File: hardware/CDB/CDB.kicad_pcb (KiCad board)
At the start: 2 copper layers, 17 parts, among them J1 Servo Motor, J2 Bateria, J3 Antena LoRa, Q1 BC547, U1 ESP32-C3, U2 RFM95W, U3 GPS, U4 BMP280, U5 GY-521

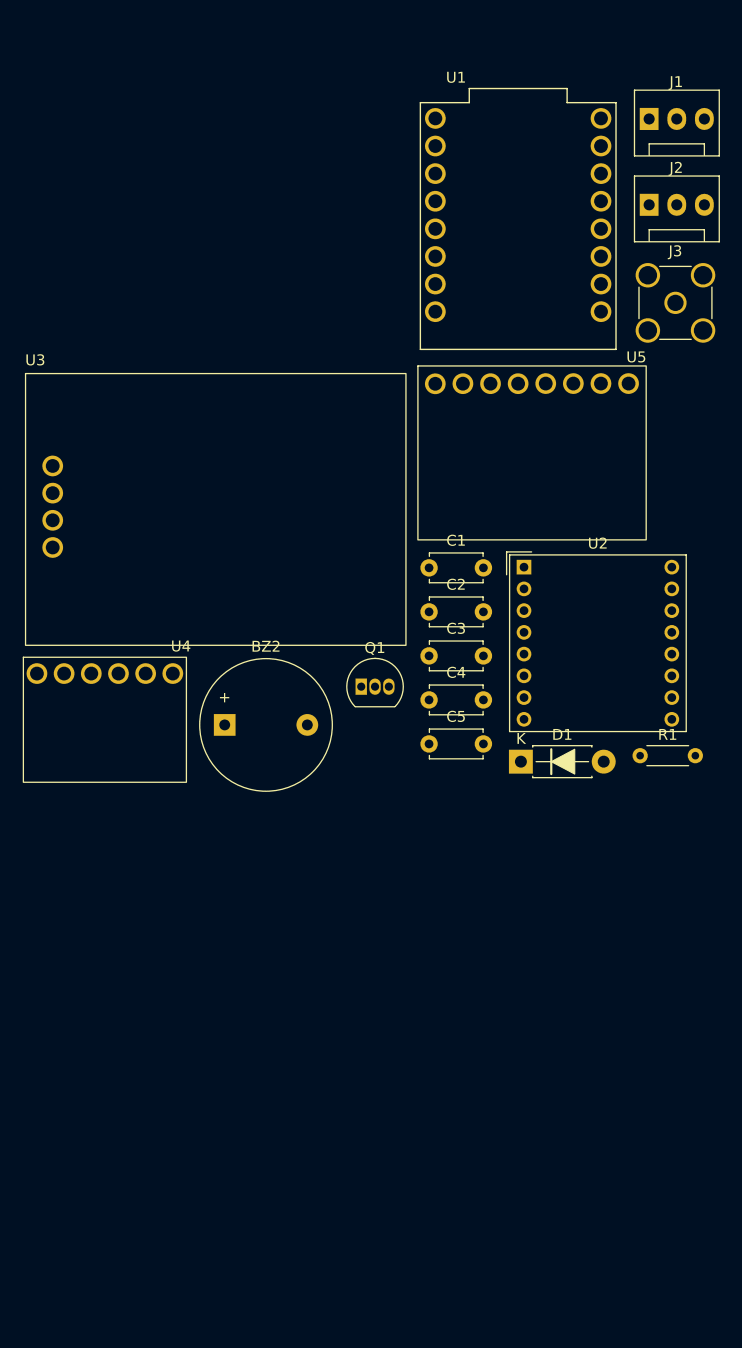
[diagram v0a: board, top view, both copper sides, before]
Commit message: add velocity threshold
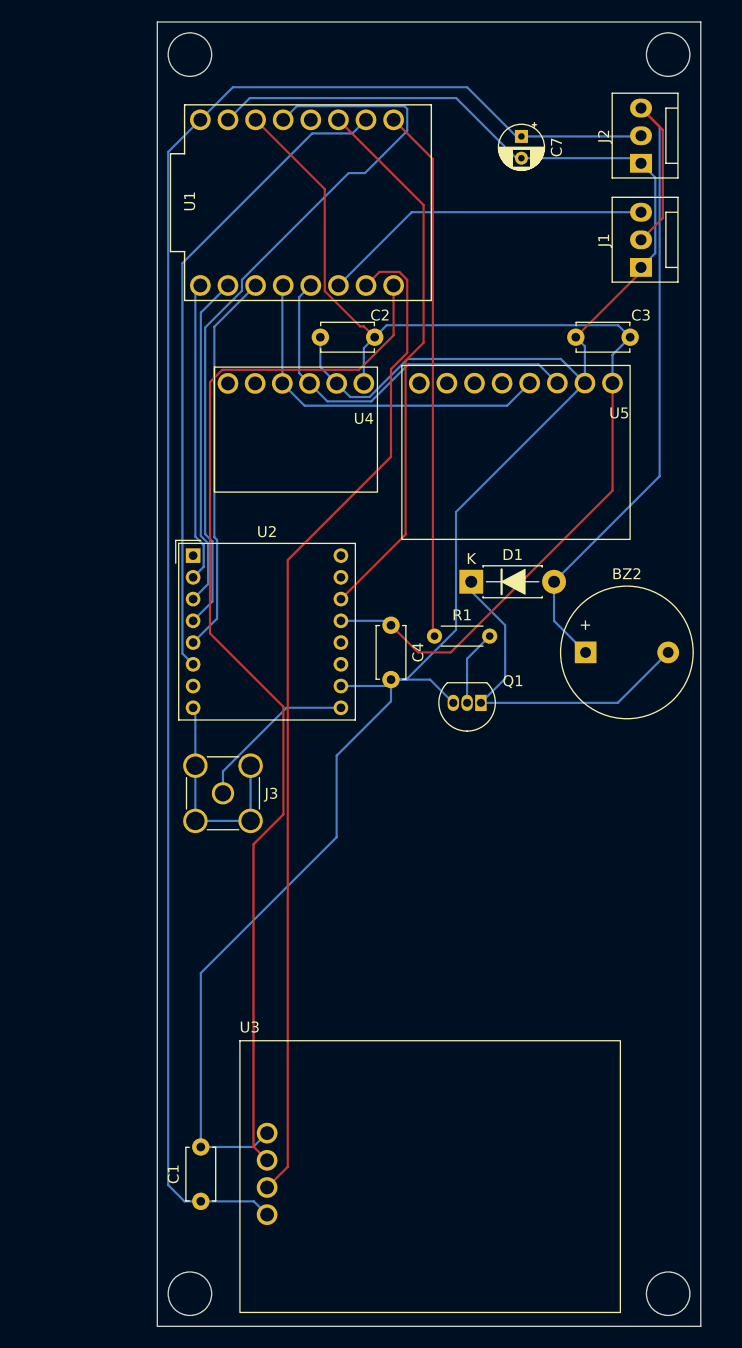
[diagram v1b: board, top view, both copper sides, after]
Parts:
- removed C5: 100nF, Capacitor_THT:C_Disc_D4.7mm_W2.5mm_P5.00mm
- added C7: 10uF, PCM_Capacitor_THT_AKL:CP_Radial_D4.0mm_P2.00mm, F.Cu at (163.5, 40.5)
- moved U3 64.5 mm to (137.6, 123.7)
- moved C1 61.9 mm to (134.0, 138.5), turned to 90 degrees
- moved J3 61.4 mm to (136.0, 101.0)
- moved C3 34.7 mm to (173.5, 59.0), turned to 180 degrees
- moved BZ2 33.9 mm to (169.4, 88.0)
- moved U4 32.0 mm to (142.8, 66.8)
- moved U2 30.5 mm to (133.3, 79.1)
- moved C2 25.8 mm to (150.0, 59.0), turned to 180 degrees
- moved R1 21.9 mm to (155.5, 86.5)
- moved U1 19.5 mm to (143.9, 46.6), turned to 90 degrees
- moved D1 17.2 mm to (158.9, 81.5)
- moved J1 13.7 mm to (174.5, 52.6), turned to 90 degrees
- moved Q1 11.1 mm to (159.8, 92.6), turned to 180 degrees
- moved C4 7.71 mm to (151.5, 85.5), turned to -90 degrees
- moved J2 3.89 mm to (174.5, 43.0), turned to 90 degrees
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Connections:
- C1 pad 2: Net-(J1-Pin_3) -> Net-(J1-Pin_1)
- C2 pad 2: Net-(J1-Pin_3) -> Net-(J1-Pin_1)
- C3 pad 2: Net-(J1-Pin_3) -> Net-(J1-Pin_1)
- C4 pad 2: Net-(J1-Pin_3) -> Net-(J1-Pin_1)
- J2 pad 1: Net-(J1-Pin_3) -> Net-(J1-Pin_1)
- Q1 pad 3: Net-(J1-Pin_3) -> Net-(J1-Pin_1)
- U1 pad 10: Net-(J1-Pin_1) -> Net-(J1-Pin_3)
- U1 pad G: Net-(J1-Pin_3) -> Net-(J1-Pin_1)
- U2 pad 10: Net-(J1-Pin_3) -> Net-(J1-Pin_1)
- U3 pad 1: Net-(J1-Pin_3) -> Net-(J1-Pin_1)
- U4 pad 2: Net-(J1-Pin_3) -> Net-(J1-Pin_1)
- U5 pad 2: Net-(J1-Pin_3) -> Net-(J1-Pin_1)
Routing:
- net Net-(J1-Pin_1): track 0.00 -> 202.7 mm
- net Net-(J2-Pin_2): track 0.00 -> 153.3 mm
- net Net-(U1-3V3): track 0.00 -> 101.0 mm
- net Net-(U1-GPIO21): track 0.00 -> 99.3 mm
- net Net-(U1-GPIO20): track 0.00 -> 93.5 mm
- net Net-(BZ2-+): track 0.00 -> 69.8 mm
- net Net-(U1-GPIO4): track 0.00 -> 68.7 mm
- net Net-(U1-GPIO1): track 0.00 -> 59.7 mm
- net Net-(U1-GPIO2): track 0.00 -> 50.5 mm
- net Net-(U1-GPIO0): track 0.00 -> 49.1 mm
- net Net-(U1-GPIO9): track 0.00 -> 35.5 mm
- net Net-(U1-GPIO7): track 0.00 -> 35.4 mm
- net Net-(U1-GPIO8): track 0.00 -> 33.5 mm
- net Net-(BZ2--): track 0.00 -> 32.5 mm
- net Net-(U1-GPIO6): track 0.00 -> 30.7 mm
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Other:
- board outline added: 50 x 120 mm
